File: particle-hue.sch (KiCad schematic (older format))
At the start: 31 parts, among them P1 MOTION_SENSOR, P2 TEMP_SENSOR, SW1 SW_PUSH, SW2 SW_PUSH, SW3 SW_PUSH, SW4 SW_PUSH, SW5 SW_PUSH, SW6 SW_PUSH, U1 PHOTON

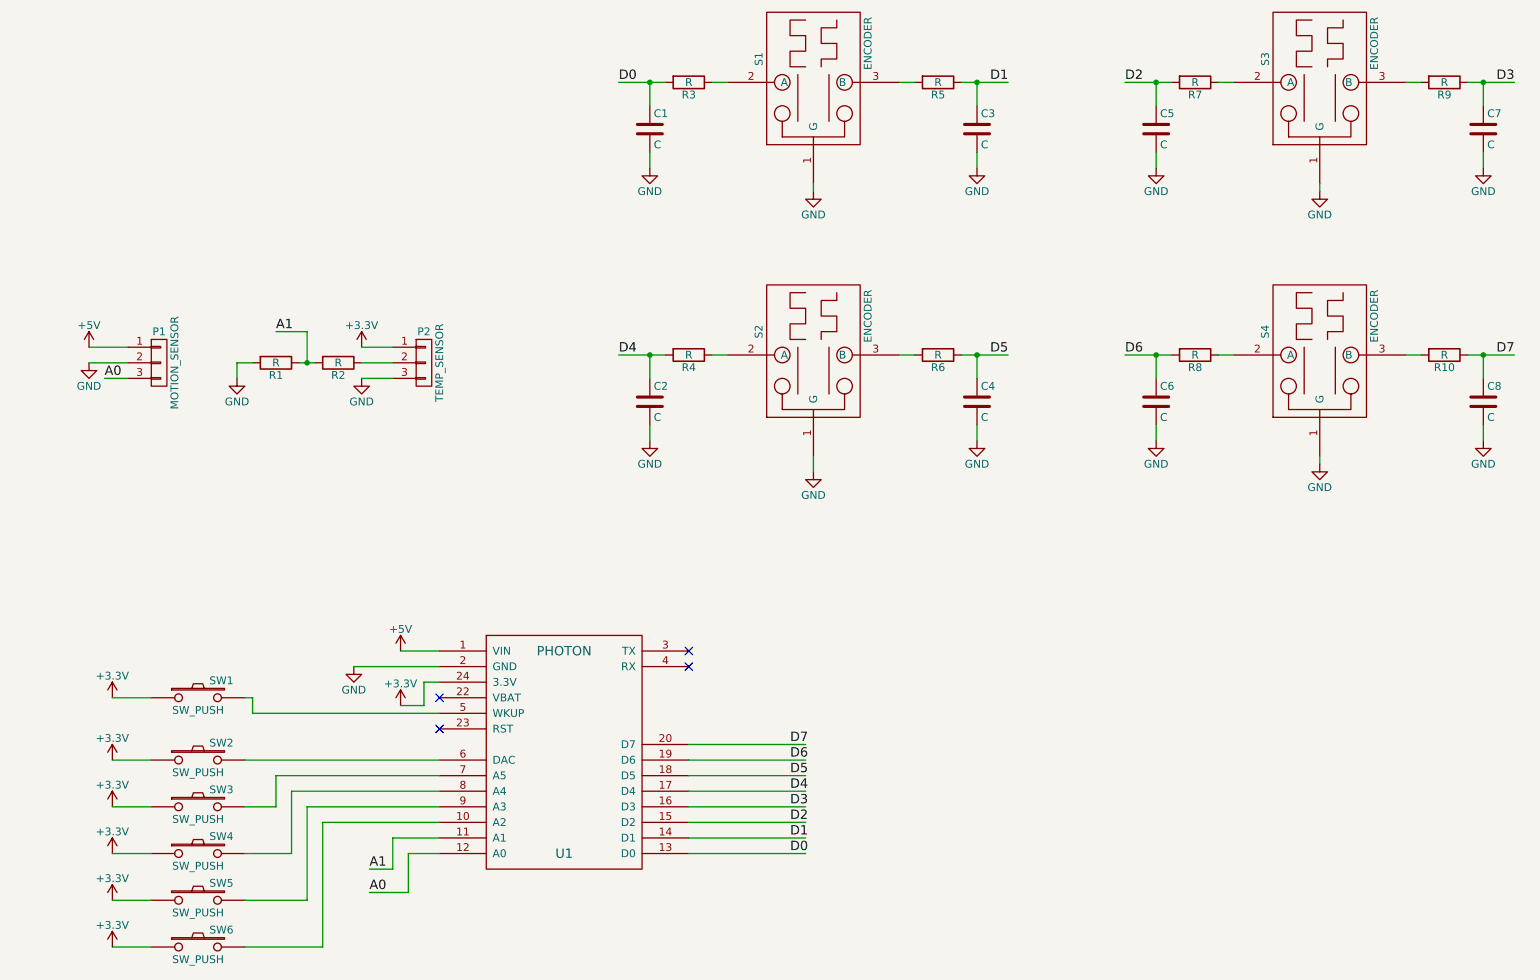
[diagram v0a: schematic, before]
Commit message: updated to reflect some changes to the software
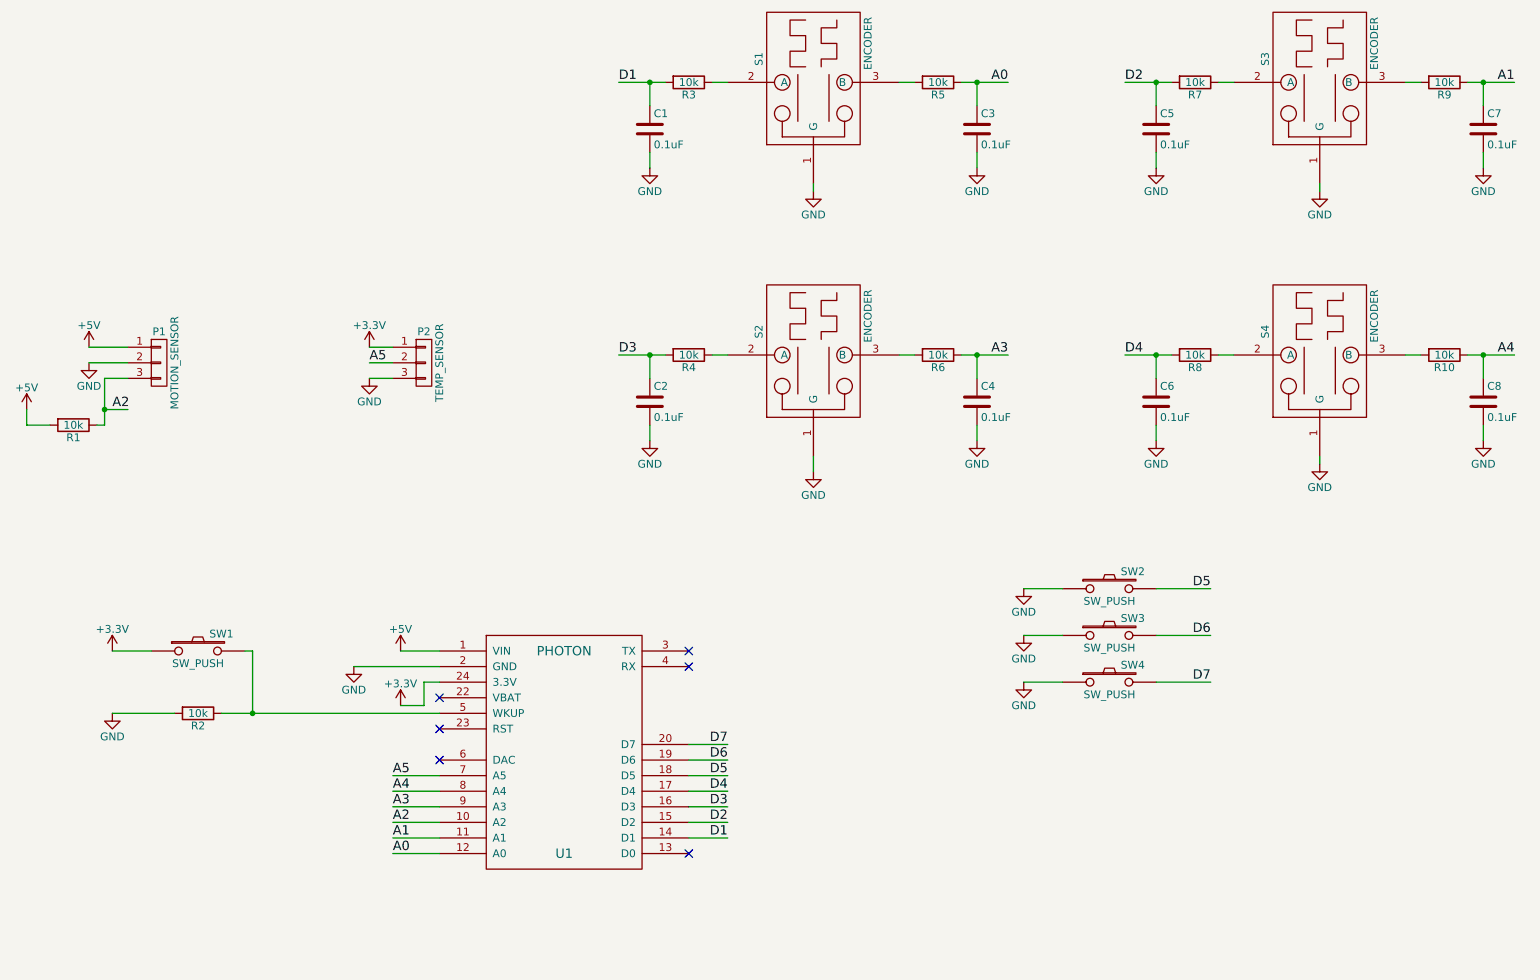
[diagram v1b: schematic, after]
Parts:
- removed SW5, SW6: SW_PUSH, Pin_Headers:Pin_Header_Straight_1x02, symbol SW_PUSH
- C1, C2, C3, C4, C5, C6, C7, C8: value C -> 0.1uF
- R1, R10, R2, R3, R4, R5, R6, R7, R8, R9: value R -> 10k
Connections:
- net labels added: A2, A3, A4, A5
- net labels removed: D0
- wire segments 88 -> 76
- no-connect marks 4 -> 6
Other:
- moved on the sheet: SW1, SW2, SW3, SW4
